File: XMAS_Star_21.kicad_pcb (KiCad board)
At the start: 4 copper layers, 80 x 148.3 mm, 64 parts, among them J1 USB_B_Micro, J2 Conn_02x01, J3 Conn_02x03_Odd_Even, J4 Conn_01x01_Female, Q1 Q_PMOS_GDS, Q2 FS8205a, SW1 SW_SPDT, U1 ATtiny1607-M, U2 NPIC6C596A, U3 NPIC6C596A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

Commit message: Added AW9523b and routing to PCB
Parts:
- removed C3: C, Capacitor_SMD:C_0603_1608Metric
- removed R1, R2, R3, R4: 100K, Resistor_SMD:R_0603_1608Metric
- removed U3: NPIC6C596A, UserFootprints:DHVQFN-16_EP_3.6x2.6_Pitch0.5mm
- U2: value NPIC6C596A -> AW9523b; footprint UserFootprints:DHVQFN-16_EP_3.6x2.6_Pitch0.5mm -> Package_DFN_QFN:QFN-24-1EP_4x4mm_P0.5mm_EP2.7x2.7mm_ThermalVias
- moved C2 26.1 mm to (100.0, 135.0), turned to 0 degrees
- moved C1 23.4 mm to (105.8, 127.5)
- moved U2 19.1 mm to (105.8, 122.7), turned to 180 degrees
- moved D31 0.22 mm to (100.0, 82.2)
- moved D32 0.22 mm to (100.0, 82.2)
- renumbered CHG to D33, STDBY to D34, TOG to JP1, AHLB to JP2
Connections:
- D25 pad 1: Net-(D25-Pad1) -> SPairYZ1
- D26 pad 1: Net-(D25-Pad1) -> SPairYZ1
- J2 pad 3: GND -> (no net)
- U1 pad 12: SR_OUTPUT_ -> Net-(U1-Pad12)
- U1 pad 13: SR_Reset_ -> Net-(U1-Pad13)
- U1 pad 14: SR_STORE -> RSTN
- U1 pad 15: SR_CLK -> SDA
- U1 pad 16: SR-DATA -> SCL
- U2 pad 1: +3V3 -> PairZX1
- U2 pad 10: SR_STORE -> PairXY1
- U2 pad 12: PairXY1 -> PairYZ1
- U2 pad 13: PairYZ1 -> PairZX0
- U2 pad 14: PairZX0 -> SPairYZ1
- U2 pad 15: SR_CLK -> SPairZX0
- U2 pad 16: GND -> SPairZX1
- U2 pad 17: GND -> CentrePair
- U2 pad 2: SR-DATA -> SPairXY0
- U2 pad 3: PairX -> SPairXY1
- U2 pad 4: PairY -> SPairYZ0
- U2 pad 5: PairZ -> PairX
- U2 pad 6: PairXY0 -> PairY
- U2 pad 7: SR_Reset_ -> PairZ
- U2 pad 8: SR_OUTPUT_ -> PairXY0
- U2 pad 9: Net-(U2-Pad9) -> GND
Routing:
- net SPairYZ1: track 0.00 -> 109.3 mm, vias 0 -> 1
- net Net-(D25-Pad1): track 65.7 -> 0.00 mm
- net SR_CLK: track 56.3 -> 0.00 mm, vias 3 -> 0
- net SR_OUTPUT_: track 52.6 -> 0.00 mm, vias 3 -> 0
- net SR_Reset_: track 52.4 -> 0.00 mm, vias 3 -> 0
- net SR_STORE: track 46.1 -> 0.00 mm, vias 3 -> 0
- net PairXY0: track 76.8 -> 109.8 mm
- net Net-(U2-Pad9): track 31.9 -> 0.00 mm, vias 2 -> 0
- net PairX: track 53.3 -> 84.4 mm
- net PairY: track 109.4 -> 137.8 mm
- net PairZ: track 92.5 -> 120.3 mm
- net +3V3: track 79.2 -> 106.4 mm
- net SR-DATA: track 23.1 -> 0.00 mm, vias 2 -> 0
- net PairXY1: track 71.5 -> 94.6 mm
- net CentrePair: track 43.0 -> 59.4 mm
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
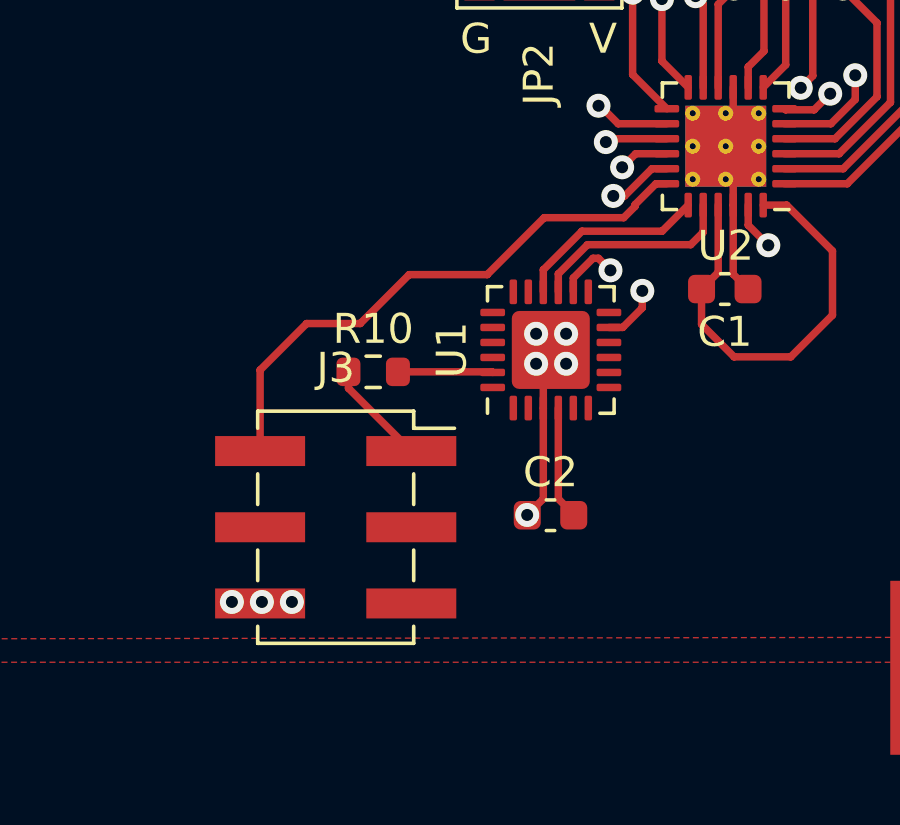
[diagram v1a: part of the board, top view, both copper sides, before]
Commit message: cleaned up UDPI connector
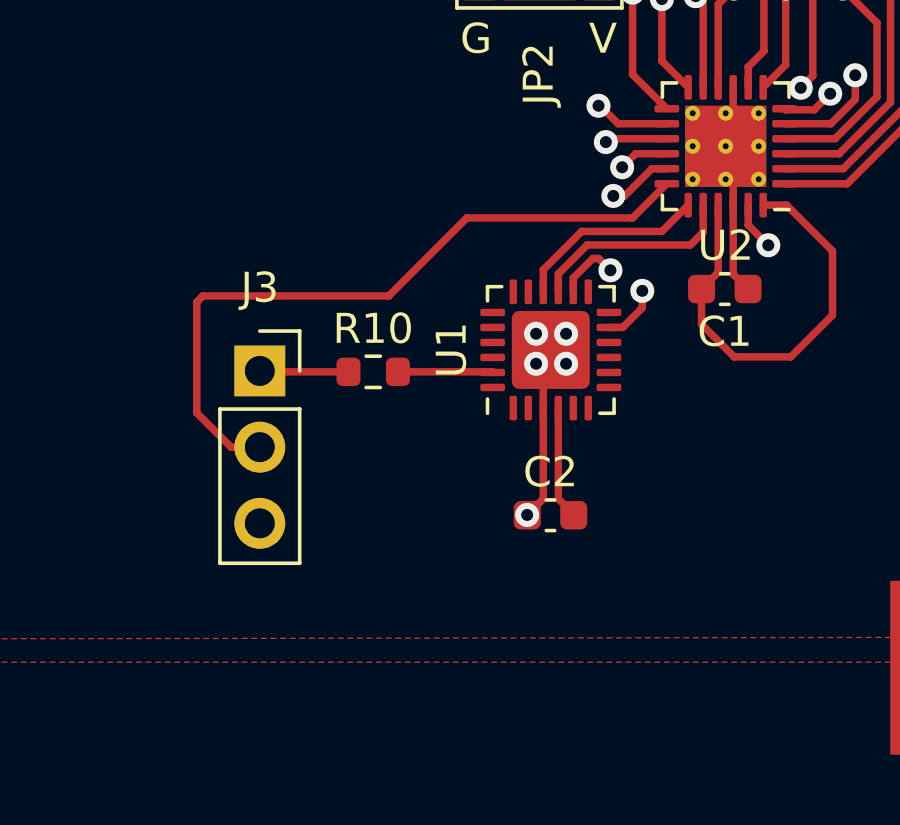
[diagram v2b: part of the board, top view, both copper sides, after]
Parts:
- J3: value Conn_02x03_Odd_Even -> Conn_01x03_Female; footprint Connector_PinSocket_2.54mm:PinSocket_2x03_P2.54mm_Vertical_SMD -> Connector_PinSocket_2.54mm:PinSocket_1x03_P2.54mm_Vertical
- moved J3 5.79 mm to (90.3, 130.2)
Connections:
- J1 pad 2: Net-(J1-Pad2) -> (no net)
- J1 pad 3: Net-(J1-Pad3) -> (no net)
- J1 pad 4: Net-(J1-Pad4) -> (no net)
- J3 pad 3: Net-(J3-Pad3) -> GND
- SW1 pad 1: Net-(SW1-Pad1) -> (no net)
- U1 pad 1: Net-(U1-Pad1) -> (no net)
- U1 pad 10: Net-(U1-Pad10) -> (no net)
- U1 pad 12: Net-(U1-Pad12) -> (no net)
- U1 pad 13: Net-(U1-Pad13) -> (no net)
- U1 pad 17: Net-(U1-Pad17) -> (no net)
- U1 pad 18: Net-(U1-Pad18) -> (no net)
- U1 pad 19: Net-(U1-Pad19) -> (no net)
- U1 pad 2: Net-(U1-Pad2) -> (no net)
- U1 pad 20: Net-(U1-Pad20) -> (no net)
- U1 pad 21: Net-(U1-Pad21) -> (no net)
- U1 pad 22: Net-(U1-Pad22) -> (no net)
- U1 pad 24: Net-(U1-Pad24) -> (no net)
- U1 pad 5: Net-(U1-Pad5) -> (no net)
- U1 pad 6: Net-(U1-Pad6) -> (no net)
- U1 pad 7: Net-(U1-Pad7) -> (no net)
- U1 pad 8: Net-(U1-Pad8) -> (no net)
- U1 pad 9: Net-(U1-Pad9) -> (no net)
- U5 pad 4: Net-(U5-Pad4) -> (no net)
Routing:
- net +3V3: track 106.4 -> 109.6 mm
- net UPDI: track 3.51 -> 2.97 mm
- net GND: vias 81 -> 78

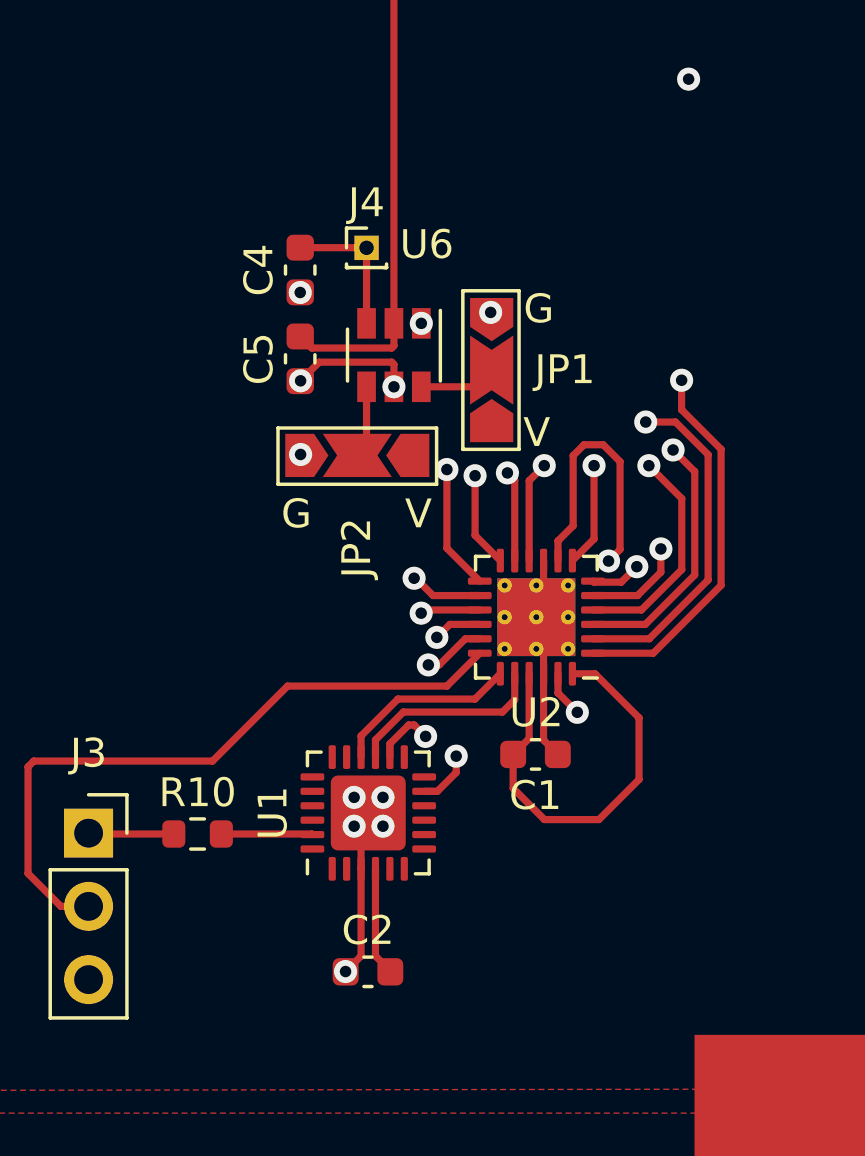
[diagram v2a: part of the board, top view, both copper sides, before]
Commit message: tidy power to ICs and start code
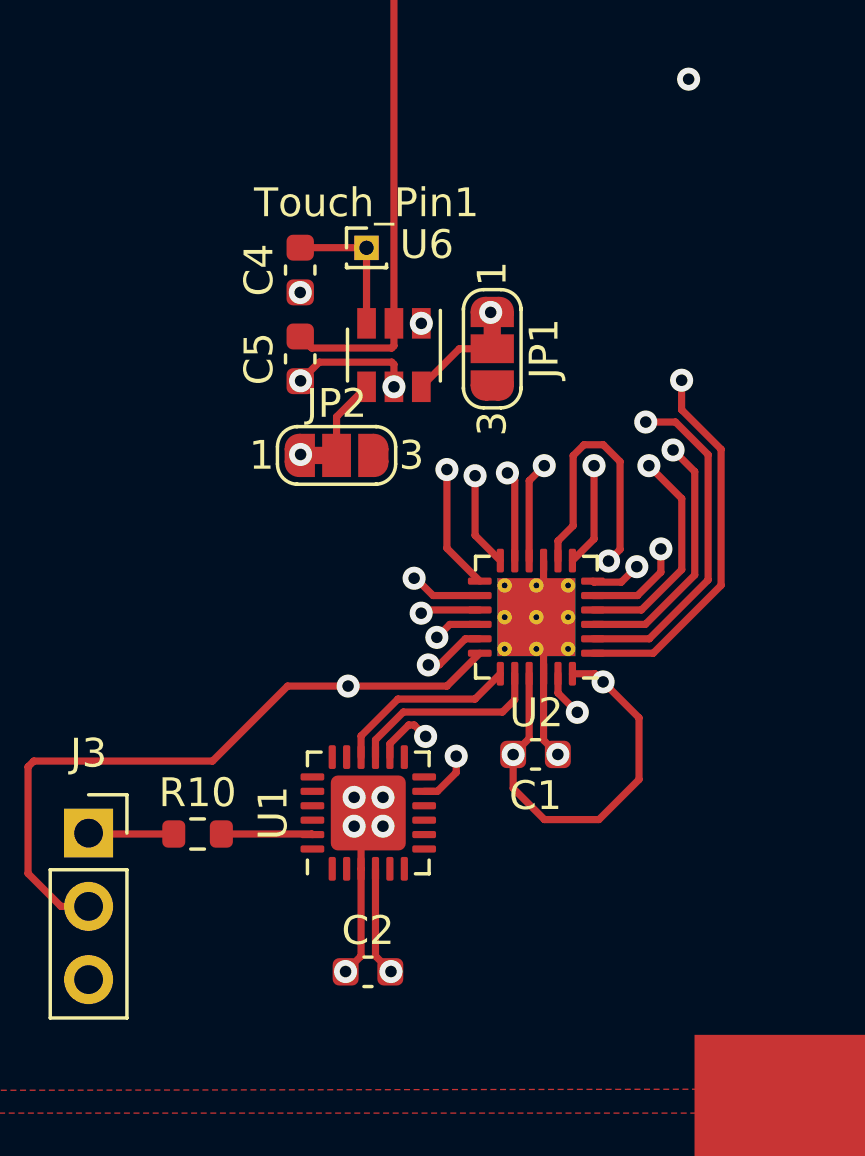
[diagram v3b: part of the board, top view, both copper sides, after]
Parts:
- JP1, JP2: value SolderJumper_3_Open -> SolderJumper_3_Bridged12; footprint Jumper:SolderJumper-3_P2.0mm_Open_TrianglePad1.0x1.5mm_NumberLabels -> Jumper:SolderJumper-3_P1.3mm_Bridged12_RoundedPad1.0x1.5mm_NumberLabels
- Touch_Pin1: renamed from J4; value Conn_01x01_Female -> Touch_Pin
- moved JP1 0.74 mm to (104.3, 113.4), turned to 270 degrees
- moved JP2 0.72 mm to (98.9, 117.1), turned to 0 degrees
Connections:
- JP1 pad 1: +3V3 -> GND
- JP1 pad 3: GND -> +3V3
- JP2 pad 1: +3V3 -> GND
- JP2 pad 3: GND -> +3V3
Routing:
- net +3V3: vias 1 -> 5
- net GND: vias 78 -> 79

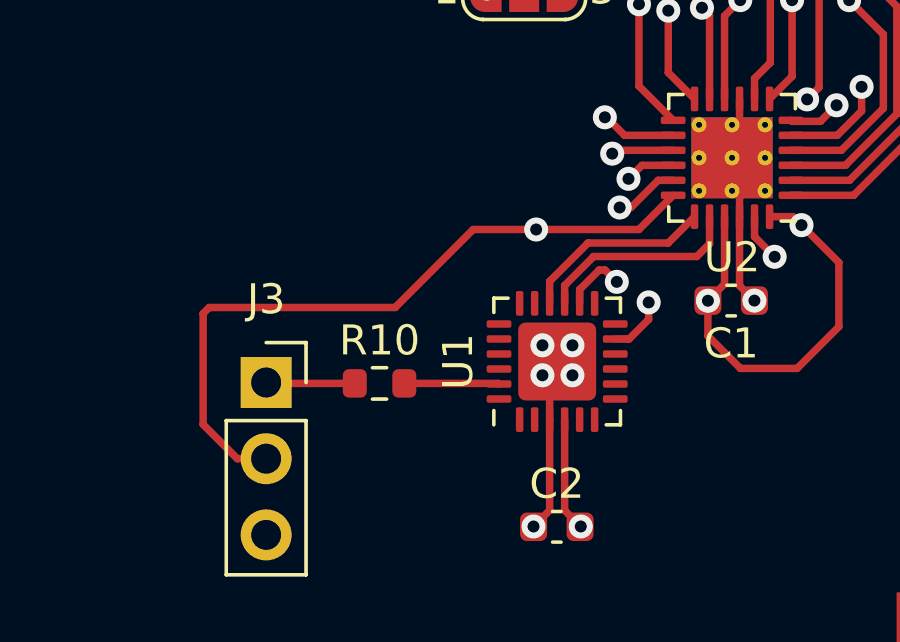
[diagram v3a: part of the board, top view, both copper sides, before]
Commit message: Remembering to put pullups on the i2cgit add --all
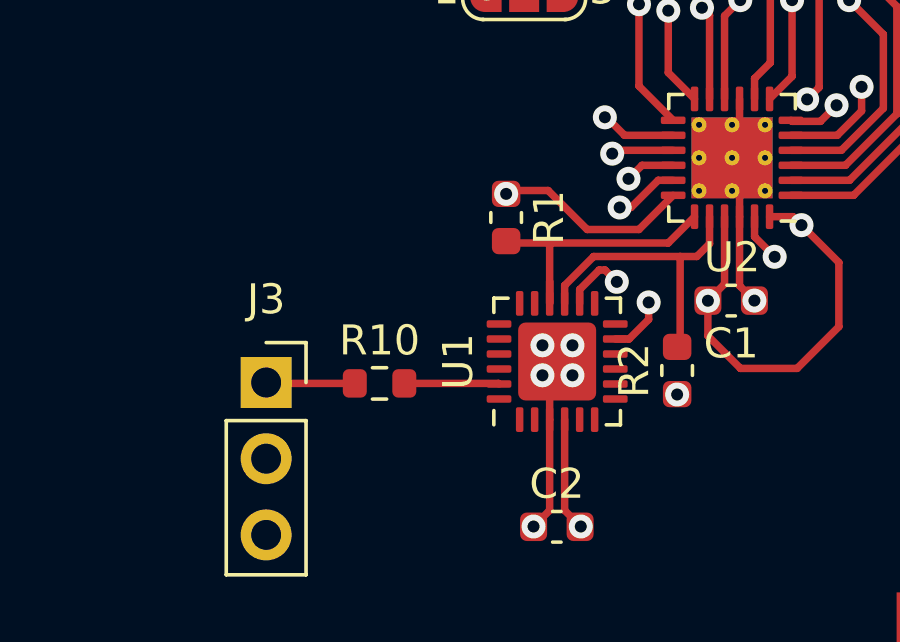
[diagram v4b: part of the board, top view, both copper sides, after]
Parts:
- added R1: R, Resistor_SMD:R_0603_1608Metric, F.Cu at (98.3, 124.7)
- added R2: R, Resistor_SMD:R_0603_1608Metric, F.Cu at (104.0, 129.8)
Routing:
- net +3V3: track 109.6 -> 92.7 mm, vias 5 -> 6
- net SDA: track 6.91 -> 9.96 mm
- net SCL: track 6.46 -> 9.42 mm

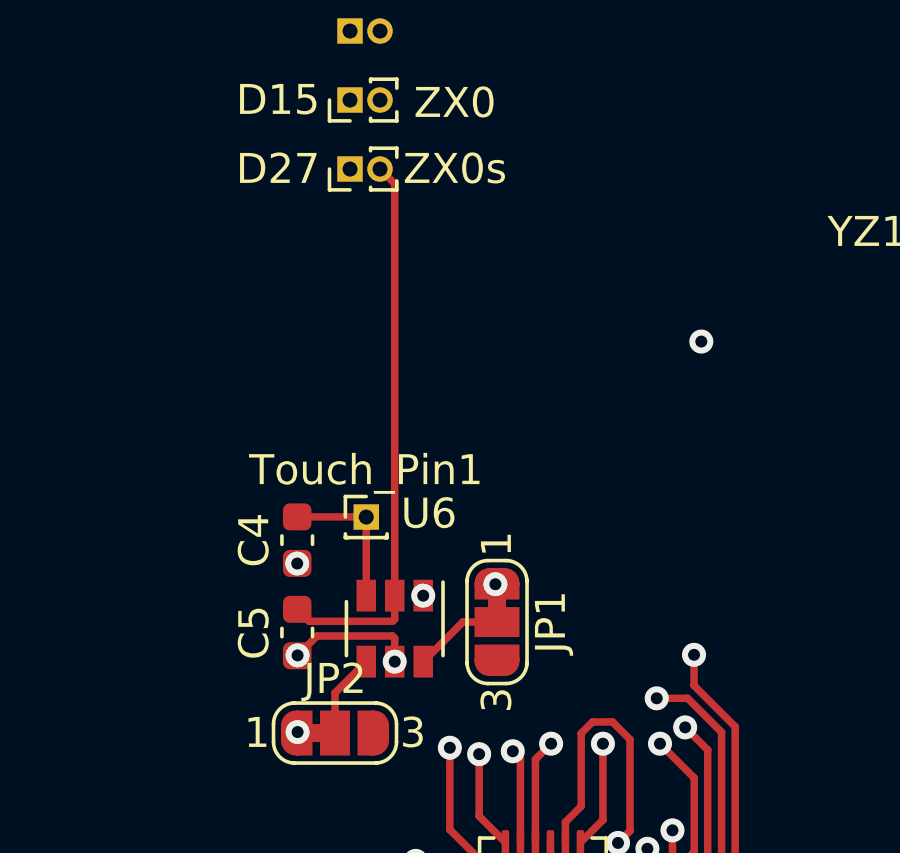
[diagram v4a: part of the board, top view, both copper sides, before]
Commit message: further shaping of the code and change TTP223 from direct to toggle output
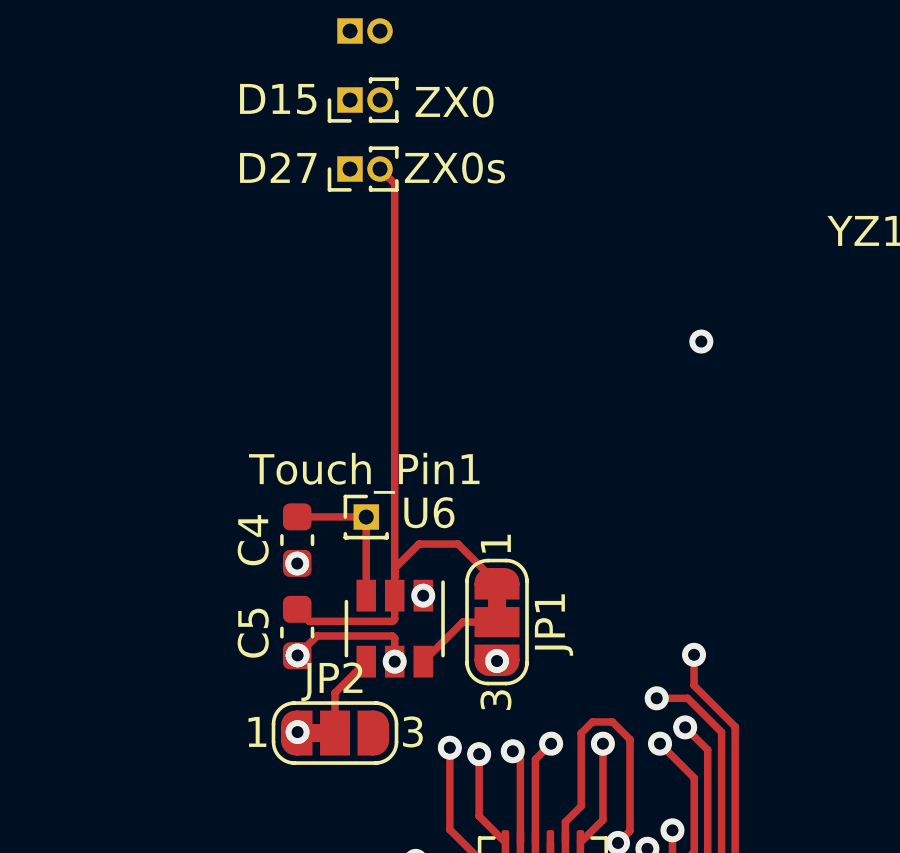
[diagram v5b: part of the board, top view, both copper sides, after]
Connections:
- JP1 pad 1: GND -> +3V3
- JP1 pad 3: +3V3 -> GND
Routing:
- net +3V3: track 92.7 -> 97.6 mm
